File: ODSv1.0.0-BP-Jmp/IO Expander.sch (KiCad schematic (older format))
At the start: 23 parts, among them J20 Conn_02x10_Odd_Even, J21 Conn_02x10_Odd_Even, U3 MAX7317, U4 NC7SZ125, U5 MAX7317, U6 NC7SZ125, U7 AD7689xCP

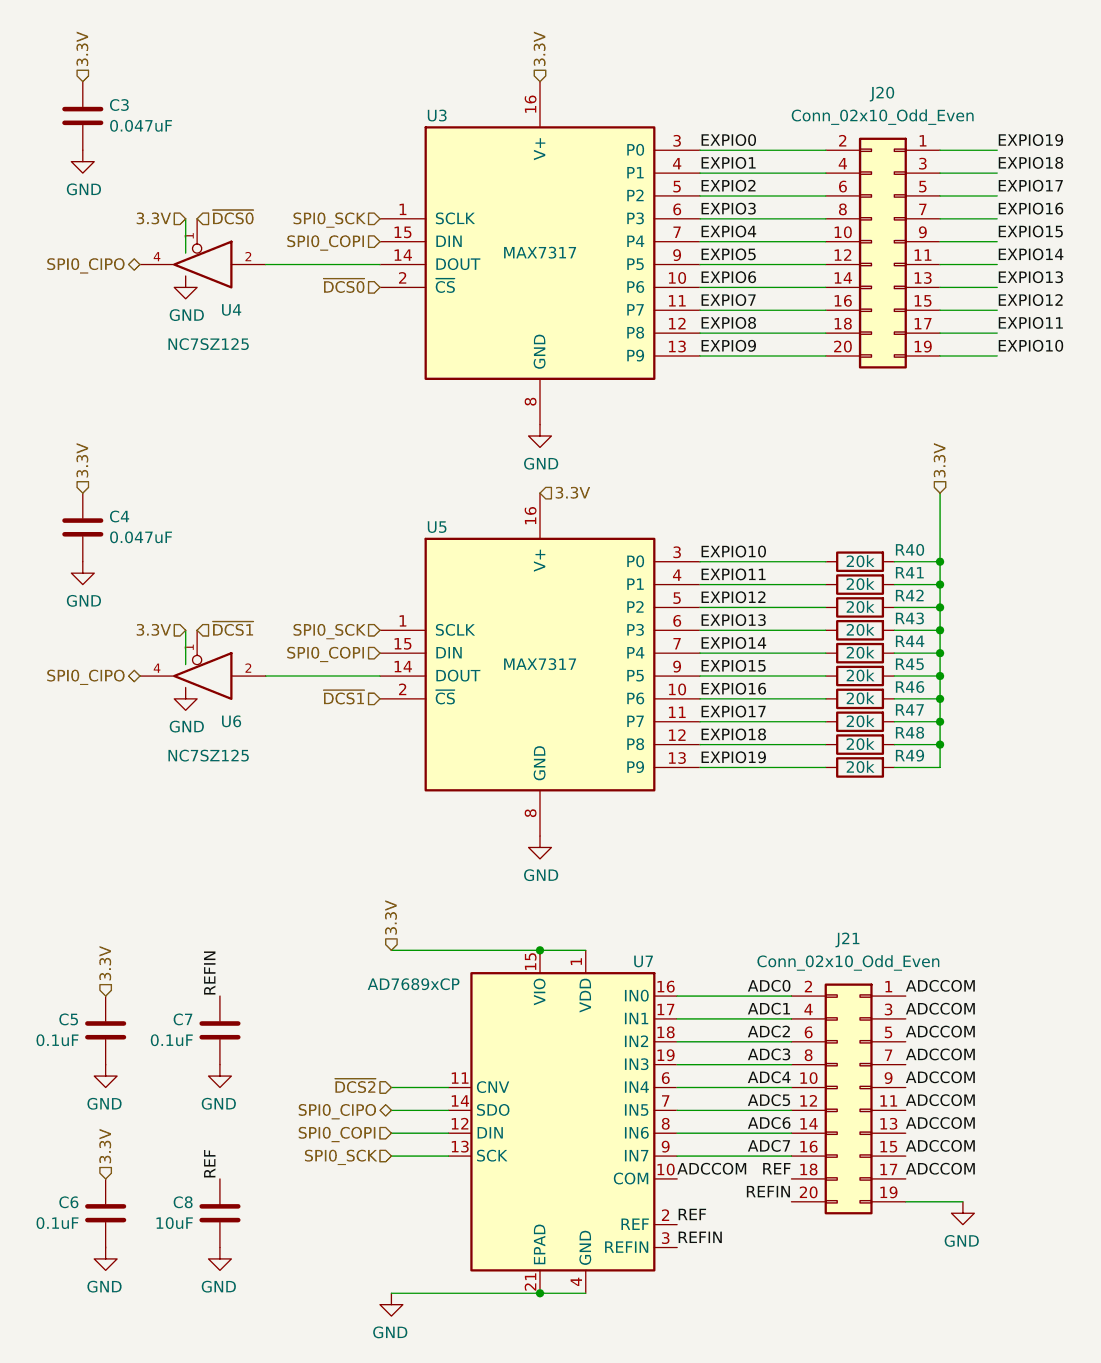
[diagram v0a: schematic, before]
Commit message: Insert 3-state buffers between all MAX7317 DOUTs and CIPO (#16)
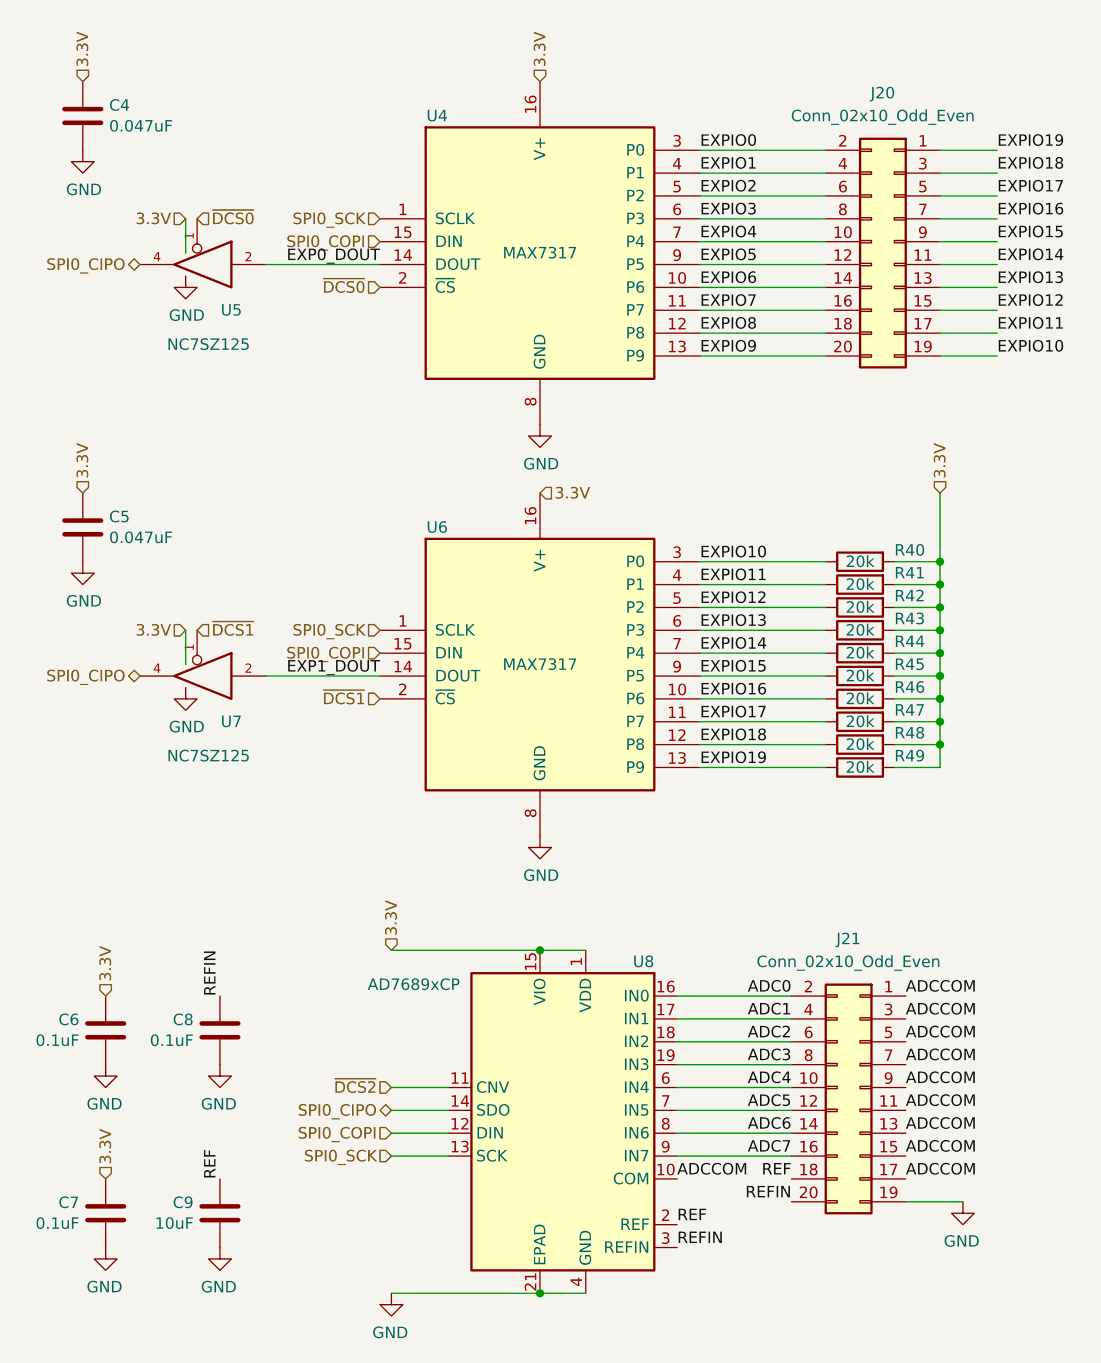
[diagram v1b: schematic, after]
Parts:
- renumbered C3 to C4, C4 to C5, C5 to C6, C6 to C7, C7 to C8, C8 to C9, U3 to U4, U4 to U5, U5 to U6, U6 to U7, U7 to U8
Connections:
- net EXP1_DOUT: now reaches U6.14 (DOUT), U7.2
- net EXP0_DOUT: now reaches U4.14 (DOUT), U5.2
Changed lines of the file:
@@
 P 750 1150
 AR Path="/60C51399/6199D8B6/60C61D72" Ref="C?"  Part="1"
-AR Path="/60C384EE/60C61D72" Ref="C3"  Part="1"
-F 0 "C3" H 865 1196 50  0000 L CNN
+AR Path="/60C384EE/60C61D72" Ref="C4"  Part="1"
+F 0 "C4" H 865 1196 50  0000 L CNN
 F 1 "0.047uF" H 865 1105 50  0000 L CNN
 F 2 "Capacitor_SMD:C_0603_1608Metric" H 788 1000 50  0001 C CNN
@@
 P 850 5150
 AR Path="/60C51399/6199D8B6/6021E777" Ref="C?"  Part="1"
-AR Path="/60C384EE/6021E777" Ref="C5"  Part="1"
-F 0 "C5" H 965 5196 50  0000 L CNN
+AR Path="/60C384EE/6021E777" Ref="C6"  Part="1"
+F 0 "C6" H 965 5196 50  0000 L CNN
 F 1 "0.1uF" H 965 5105 50  0000 L CNN
 F 2 "Capacitor_SMD:C_0603_1608Metric" H 888 5000 50  0001 C CNN
@@
 $EndComp
 $Comp
-L Octopi:AD7689xCP U7
+L Octopi:AD7689xCP U8
 U 1 1 602154C4
 P 2850 5500
-F 0 "U7" H 2450 6150 50  0000 L CNN
+F 0 "U8" H 2450 6150 50  0000 L CNN
 F 1 "AD7689xCP" H 3300 6050 50  0000 L CNN
 F 2 "Package_CSP:LFCSP-20-1EP_4x4mm_P0.5mm_EP2.5x2.5mm" H 2850 5500 50  0001 C CNN
@@
 P 1350 5950
 AR Path="/60C51399/6199D8B6/60237E52" Ref="C?"  Part="1"
-AR Path="/60C384EE/60237E52" Ref="C8"  Part="1"
-F 0 "C8" H 1465 5996 50  0000 L CNN
+AR Path="/60C384EE/60237E52" Ref="C9"  Part="1"
+F 0 "C9" H 1465 5996 50  0000 L CNN
 F 1 "10uF" H 1465 5905 50  0000 L CNN
 F 2 "Capacitor_SMD:C_0805_2012Metric" H 1388 5800 50  0001 C CNN
@@
 P 1350 5150
 AR Path="/60C51399/6199D8B6/60290679" Ref="C?"  Part="1"
-AR Path="/60C384EE/60290679" Ref="C7"  Part="1"
-F 0 "C7" H 1465 5196 50  0000 L CNN
+AR Path="/60C384EE/60290679" Ref="C8"  Part="1"
+F 0 "C8" H 1465 5196 50  0000 L CNN
 F 1 "0.1uF" H 1465 5105 50  0000 L CNN
 F 2 "Capacitor_SMD:C_0603_1608Metric" H 1388 5000 50  0001 C CNN
@@
 P 850 5950
 AR Path="/60C51399/6199D8B6/602A3F4C" Ref="C?"  Part="1"
-AR Path="/60C384EE/602A3F4C" Ref="C6"  Part="1"
-F 0 "C6" H 965 5996 50  0000 L CNN
+AR Path="/60C384EE/602A3F4C" Ref="C7"  Part="1"
+F 0 "C7" H 965 5996 50  0000 L CNN
 F 1 "0.1uF" H 965 5905 50  0000 L CNN
 F 2 "Capacitor_SMD:C_0603_1608Metric" H 888 5800 50  0001 C CNN
@@
 P 750 2950
 AR Path="/60C51399/6199D8B6/605006E9" Ref="C?"  Part="1"
-AR Path="/60C384EE/605006E9" Ref="C4"  Part="1"
-F 0 "C4" H 865 2996 50  0000 L CNN
+AR Path="/60C384EE/605006E9" Ref="C5"  Part="1"
+F 0 "C5" H 865 2996 50  0000 L CNN
 F 1 "0.047uF" H 865 2905 50  0000 L CNN
 F 2 "Capacitor_SMD:C_0603_1608Metric" H 788 2800 50  0001 C CNN
@@
 P 2750 3550
 AR Path="/60C51399/6199D8B6/605006DD" Ref="U?"  Part="1"
-AR Path="/60C384EE/605006DD" Ref="U5"  Part="1"
+AR Path="/60C384EE/605006DD" Ref="U6"  Part="1"
 AR Path="/605006DD" Ref="U?"  Part="1"
-F 0 "U5" H 2300 4150 50  0000 C CNN
+F 0 "U6" H 2300 4150 50  0000 C CNN
 F 1 "MAX7317" H 2750 3550 50  0000 C CNN
 F 2 "Package_SO:QSOP-16_3.9x4.9mm_P0.635mm" H 2950 2900 50  0001 L CNN
@@
 P 2750 1750
 AR Path="/60C51399/6199D8B6/60C56060" Ref="U?"  Part="1"
-AR Path="/60C384EE/60C56060" Ref="U3"  Part="1"
+AR Path="/60C384EE/60C56060" Ref="U4"  Part="1"
 AR Path="/60C56060" Ref="U3"  Part="1"
-F 0 "U3" H 2300 2350 50  0000 C CNN
+F 0 "U4" H 2300 2350 50  0000 C CNN
 F 1 "MAX7317" H 2750 1750 50  0000 C CNN
 F 2 "Package_SO:QSOP-16_3.9x4.9mm_P0.635mm" H 2950 1100 50  0001 L CNN
@@
 SPI0_SCK
 $Comp
-L Octopi:NC7SZ125 U4
+L Octopi:NC7SZ125 U5
 U 1 1 605F593B
 P 1250 1800
-F 0 "U4" H 1100 1600 50  0000 C CNN
+F 0 "U5" H 1100 1600 50  0000 C CNN
 F 1 "NC7SZ125" H 1200 1450 50  0000 C CNN
 F 2 "Package_TO_SOT_SMD:SOT-353_SC-70-5" H 1250 1800 50  0001 C CNN
@@
 SPI0_CIPO
 $Comp
-L Octopi:NC7SZ125 U6
+L Octopi:NC7SZ125 U7
 U 1 1 60602B26
 P 1250 3600
-F 0 "U6" H 1100 3400 50  0000 C CNN
+F 0 "U7" H 1100 3400 50  0000 C CNN
 F 1 "NC7SZ125" H 1200 3250 50  0000 C CNN
 F 2 "Package_TO_SOT_SMD:SOT-353_SC-70-5" H 1250 3600 50  0001 C CNN
@@
 	0    -1   1    0
 $EndComp
+Text Label 2050 1800 2    50   ~ 0
+EXP0_DOUT
+Text Label 2050 3600 2    50   ~ 0
+EXP1_DOUT
 $EndSCHEMATC

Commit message: Add bypass caps to the 3-state buffers for BP-Jmp's I/O expanders
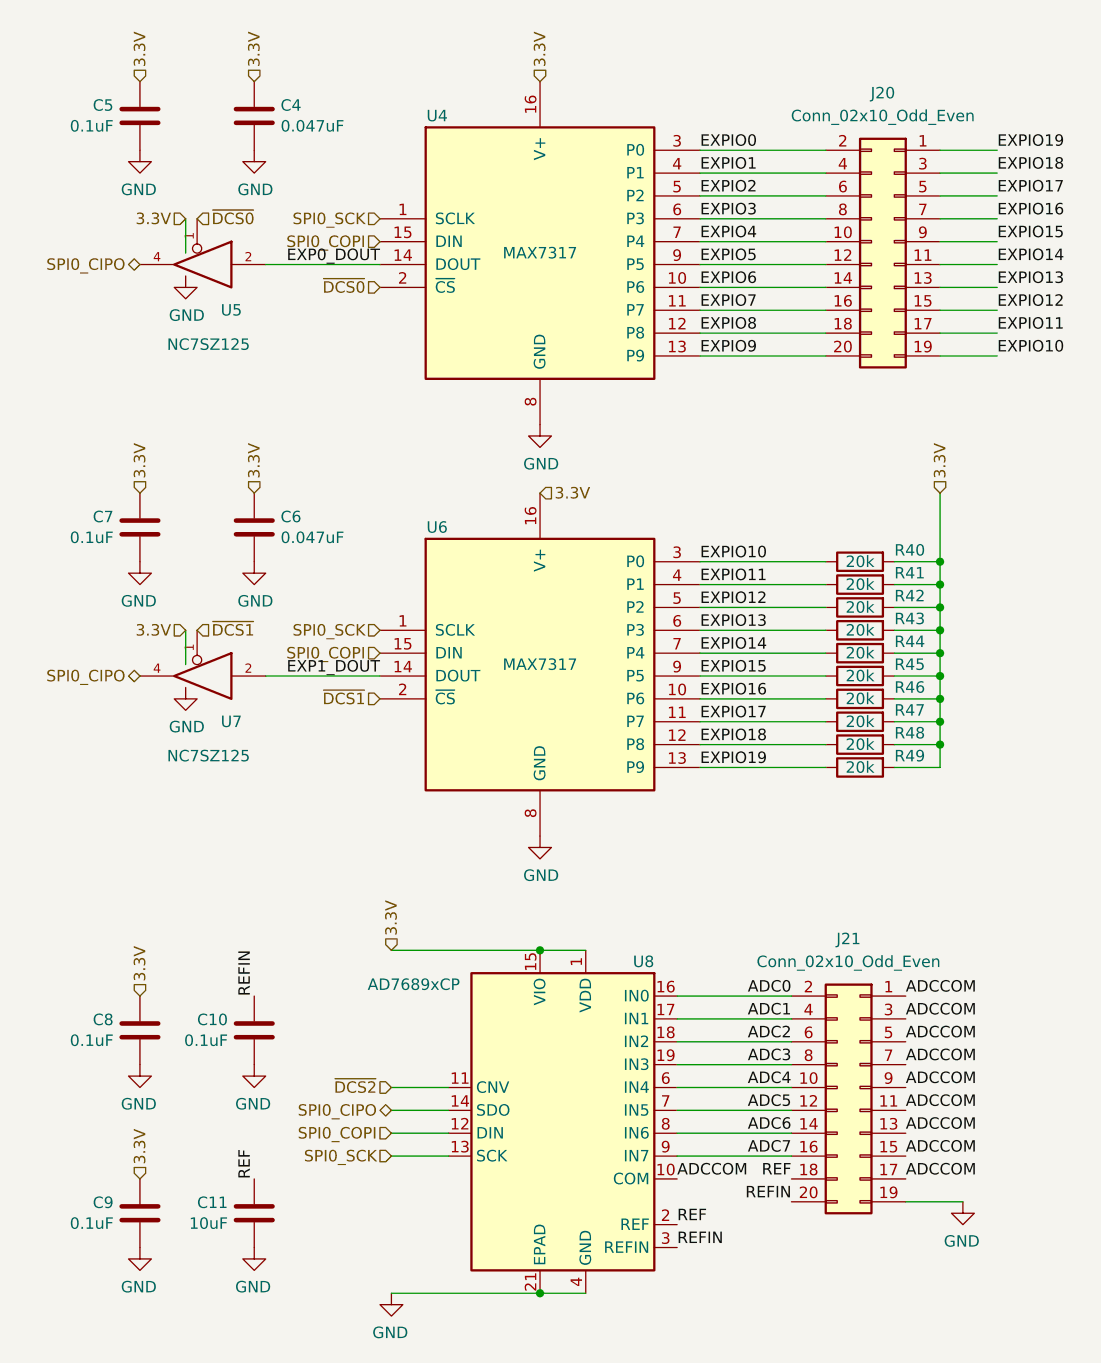
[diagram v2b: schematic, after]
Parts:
- added C6: 0.047uF, Capacitor_SMD:C_0603_1608Metric, symbol Device:C
- added C7: 0.1uF, Capacitor_SMD:C_0603_1608Metric, symbol Device:C
- C5: value 0.047uF -> 0.1uF; Digikey ID 478-1235-1-ND -> 478-7018-1-ND; MPN 06033C473KAT2A -> 06033C104KAT4A; Ordering URL https://www.digikey.com/en/products/detail/avx-corporation/06033C473KAT2A/563345 -> https://www.digikey.com/en/products/detail/avx-corporation/06033C104KAT4A/3247517
- renumbered C8 to C10, C9 to C11, C6 to C8, C7 to C9
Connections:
- net GND: now also C6.2, C7.2
- net VCC: now also C6.1, C7.1
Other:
- moved on the sheet: C10, C11, C8, C9

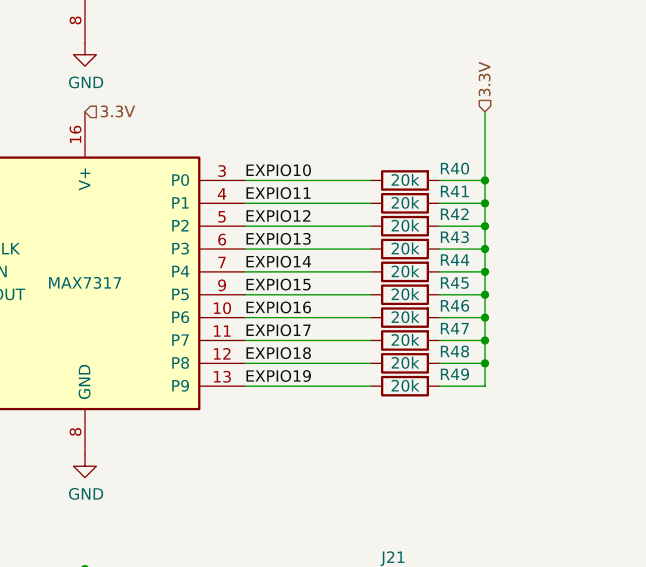
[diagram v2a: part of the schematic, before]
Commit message: Use 2k pullups instead of 20k pullups on BP-Jmp
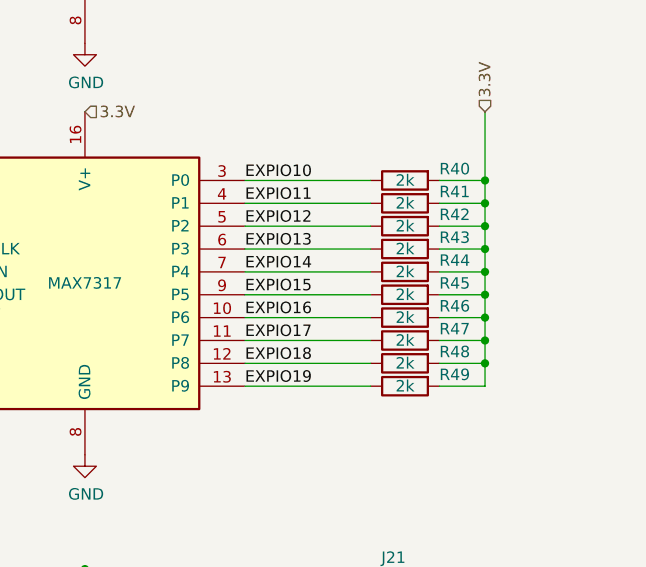
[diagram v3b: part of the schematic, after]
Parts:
- R40, R41, R42, R43, R44, R45, R46, R47, R48, R49: value 20k -> 2k; Digikey ID 311-20.0KHRCT-ND -> 311-2.00KHRCT-ND; MPN RC0603FR-0720KL -> RC0603FR-072KL; Ordering URL https://www.digikey.com/en/products/detail/yageo/RC0603FR-0720KL/727040 -> https://www.digikey.com/en/products/detail/yageo/RC0603FR-072KL/727009

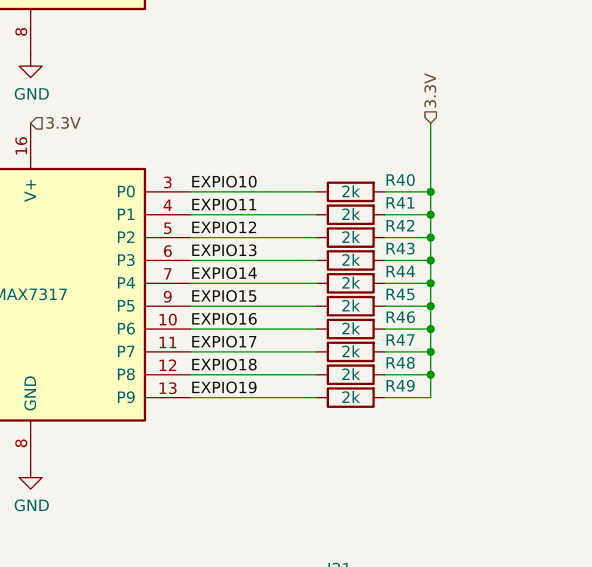
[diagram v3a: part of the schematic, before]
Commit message: Add 2k pullups within DCS selectors (#17), bump BP-Jmp to 0.2.0
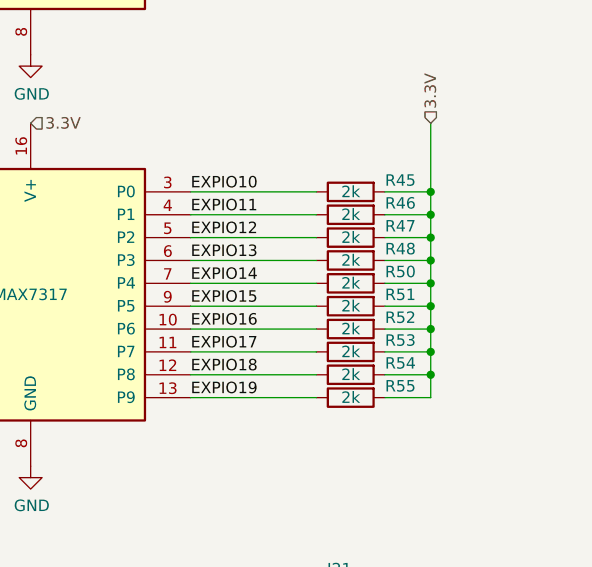
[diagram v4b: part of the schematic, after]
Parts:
- R45: renamed from R40; Digikey ID 311-2.00KHRCT-ND -> 311-20.0KHRCT-ND; MPN RC0603FR-072KL -> RC0603FR-0720KL; Ordering URL https://www.digikey.com/en/products/detail/yageo/RC0603FR-072KL/727009 -> https://www.digikey.com/en/products/detail/yageo/RC0603FR-0720KL/727040
- R46: renamed from R41; Digikey ID 311-2.00KHRCT-ND -> 311-20.0KHRCT-ND; MPN RC0603FR-072KL -> RC0603FR-0720KL; Ordering URL https://www.digikey.com/en/products/detail/yageo/RC0603FR-072KL/727009 -> https://www.digikey.com/en/products/detail/yageo/RC0603FR-0720KL/727040
- R47: renamed from R42; Digikey ID 311-2.00KHRCT-ND -> 311-20.0KHRCT-ND; MPN RC0603FR-072KL -> RC0603FR-0720KL; Ordering URL https://www.digikey.com/en/products/detail/yageo/RC0603FR-072KL/727009 -> https://www.digikey.com/en/products/detail/yageo/RC0603FR-0720KL/727040
- R48: renamed from R43; Digikey ID 311-2.00KHRCT-ND -> 311-20.0KHRCT-ND; MPN RC0603FR-072KL -> RC0603FR-0720KL; Ordering URL https://www.digikey.com/en/products/detail/yageo/RC0603FR-072KL/727009 -> https://www.digikey.com/en/products/detail/yageo/RC0603FR-0720KL/727040
- R50: renamed from R44; Digikey ID 311-2.00KHRCT-ND -> 311-20.0KHRCT-ND; MPN RC0603FR-072KL -> RC0603FR-0720KL; Ordering URL https://www.digikey.com/en/products/detail/yageo/RC0603FR-072KL/727009 -> https://www.digikey.com/en/products/detail/yageo/RC0603FR-0720KL/727040
- R51: renamed from R45; Digikey ID 311-2.00KHRCT-ND -> 311-20.0KHRCT-ND; MPN RC0603FR-072KL -> RC0603FR-0720KL; Ordering URL https://www.digikey.com/en/products/detail/yageo/RC0603FR-072KL/727009 -> https://www.digikey.com/en/products/detail/yageo/RC0603FR-0720KL/727040
- R52: renamed from R46; Digikey ID 311-2.00KHRCT-ND -> 311-20.0KHRCT-ND; MPN RC0603FR-072KL -> RC0603FR-0720KL; Ordering URL https://www.digikey.com/en/products/detail/yageo/RC0603FR-072KL/727009 -> https://www.digikey.com/en/products/detail/yageo/RC0603FR-0720KL/727040
- R53: renamed from R47; Digikey ID 311-2.00KHRCT-ND -> 311-20.0KHRCT-ND; MPN RC0603FR-072KL -> RC0603FR-0720KL; Ordering URL https://www.digikey.com/en/products/detail/yageo/RC0603FR-072KL/727009 -> https://www.digikey.com/en/products/detail/yageo/RC0603FR-0720KL/727040
- R54: renamed from R48; Digikey ID 311-2.00KHRCT-ND -> 311-20.0KHRCT-ND; MPN RC0603FR-072KL -> RC0603FR-0720KL; Ordering URL https://www.digikey.com/en/products/detail/yageo/RC0603FR-072KL/727009 -> https://www.digikey.com/en/products/detail/yageo/RC0603FR-0720KL/727040
- R55: renamed from R49; Digikey ID 311-2.00KHRCT-ND -> 311-20.0KHRCT-ND; MPN RC0603FR-072KL -> RC0603FR-0720KL; Ordering URL https://www.digikey.com/en/products/detail/yageo/RC0603FR-072KL/727009 -> https://www.digikey.com/en/products/detail/yageo/RC0603FR-0720KL/727040
